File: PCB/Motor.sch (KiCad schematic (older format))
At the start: 30 parts, among them J201 SW2, M201 Stepper_Motor_bipolar, U201 L6470_HTSSOP28

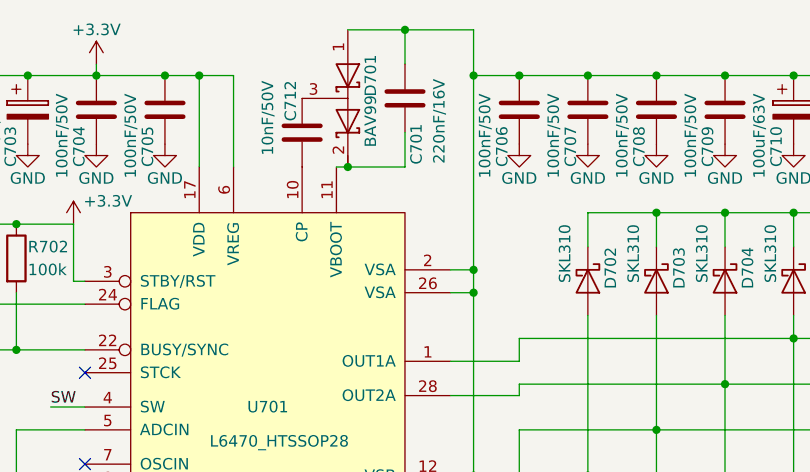
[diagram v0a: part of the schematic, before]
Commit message: Schema: fix schema ERC, connect CS, FLAG and BUSY pins to MCU, connect SPI
ERC: fixed L6470 pin types, add power flags, fixed programming
connector pin types
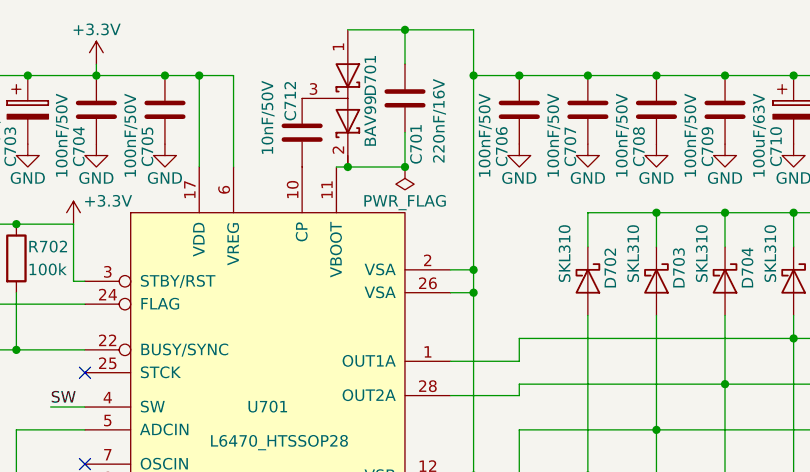
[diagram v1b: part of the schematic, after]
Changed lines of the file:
@@
 	4600 4800 4500 4800
 Connection ~ 4500 4800
+$Comp
+L power:PWR_FLAG #FLG0101
+U 1 1 5E6182B1
+P 4950 2400
+AR Path="/5D3521E4/5E6182B1" Ref="#FLG0101"  Part="1"
+AR Path="/5D4BFD94/5E6182B1" Ref="#FLG0102"  Part="1"
+AR Path="/5D4C05D6/5E6182B1" Ref="#FLG0103"  Part="1"
+AR Path="/5D4C05DE/5E6182B1" Ref="#FLG0104"  Part="1"
+AR Path="/5D4C14A6/5E6182B1" Ref="#FLG0105"  Part="1"
+AR Path="/5D4C14AE/5E6182B1" Ref="#FLG0106"  Part="1"
+F 0 "#FLG0106" H 4950 2475 50  0001 C CNN
+F 1 "PWR_FLAG" H 4950 2550 50  0000 C CNN
+F 2 "" H 4950 2400 50  0001 C CNN
+F 3 "~" H 4950 2400 50  0001 C CNN
+	1    4950 2400
+	-1   0    0    1
+$EndComp
+Connection ~ 4950 2400
 $EndSCHEMATC

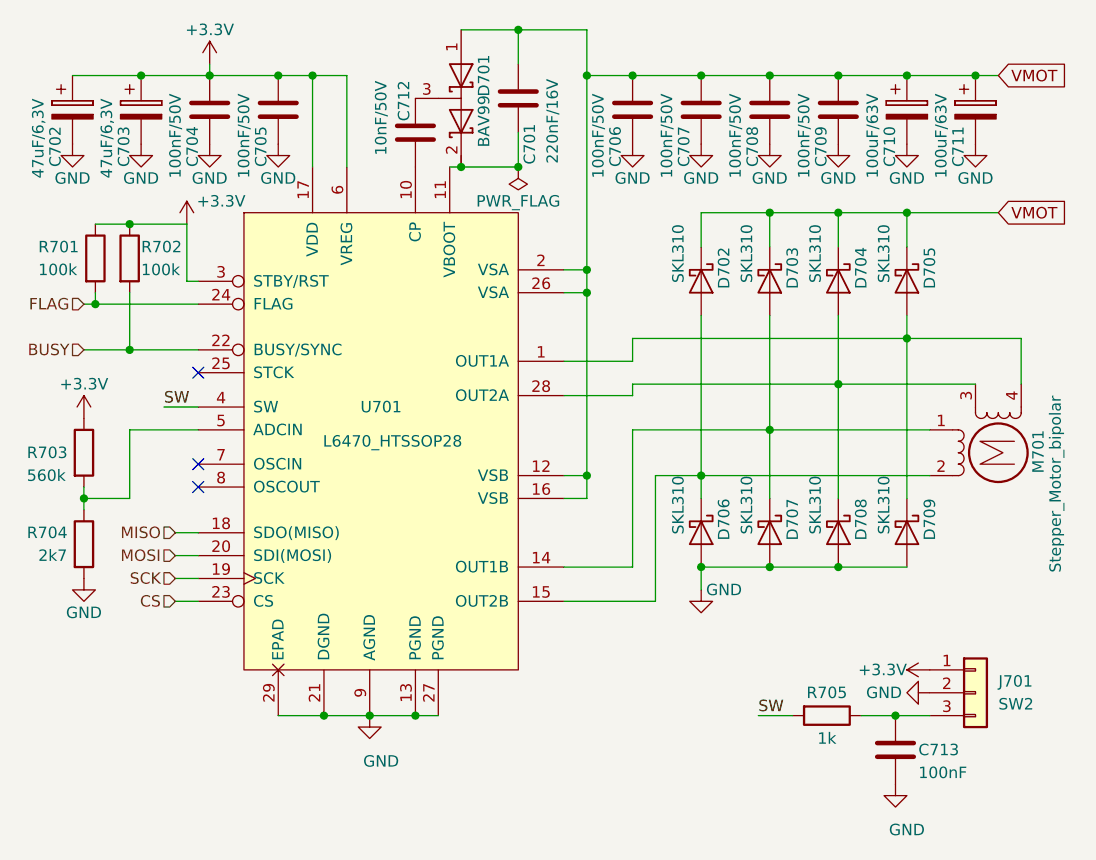
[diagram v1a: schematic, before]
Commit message: Schema&PCB: shrink board to 80x100mm, remove excessive mounting holes
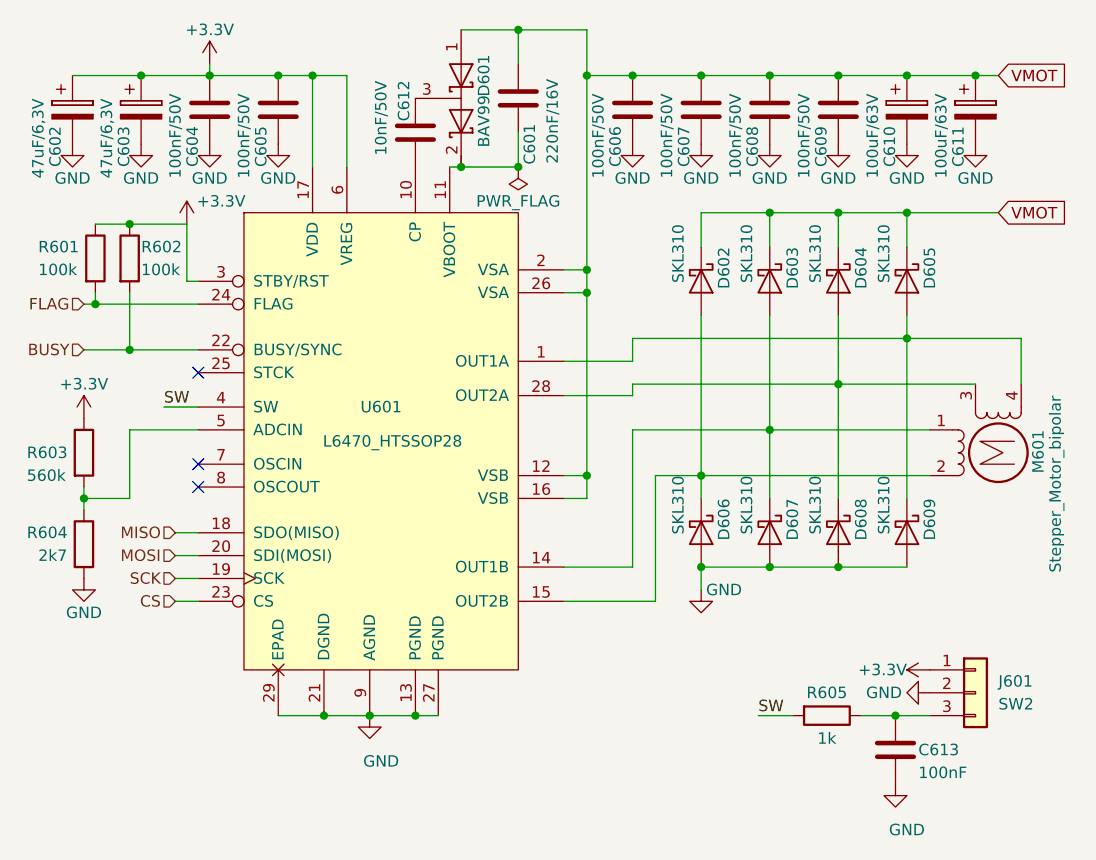
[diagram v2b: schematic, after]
